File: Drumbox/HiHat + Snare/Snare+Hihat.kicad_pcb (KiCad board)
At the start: 2 copper layers, 127.5 x 133 mm, 81 parts, among them J1 Snare IN, J2 Power Input, J3 HiHat IN, J4 Snare OUT, J5 Conn_01x08_Male, J6 Conn_01x08_Female, J7 Conn_01x08_Male, J8 Conn_01x08_Female, J9 HiHat OUT, Q1 BC546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

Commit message: lots
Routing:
- net GND: vias 10 -> 9

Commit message: finish snare + hihat
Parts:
- added REF**: Doepfer Mounting hole, Synth:Doepfer Mounting hole, F.Cu at (148.5, 22.5)
- added REF**: Doepfer Mounting hole, Synth:Doepfer Mounting hole, F.Cu at (127.0, 22.5)
- added REF**: Doepfer Mounting hole, Synth:Doepfer Mounting hole, F.Cu at (126.5, 149.5)
- added REF**: Doepfer Mounting hole, Synth:Doepfer Mounting hole, F.Cu at (148.5, 149.5)
- moved C13 0.50 mm to (83.0, 80.5)
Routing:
- net /DeH: track 56.8 -> 69.5 mm
- net /HiO: track 92.2 -> 94.1 mm
- net /SnO: track 80.5 -> 81.5 mm
- net /HiH: track 103.0 -> 103.9 mm
- net Net-(J9-PadT): track 72.7 -> 73.4 mm
- net GND: vias 9 -> 2
- net (no net): vias 7 -> 12
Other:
- outline, holes or cut-outs redrawn
- board text added: "JLCJLCJLCJLC"

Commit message: fix gerber files on ms20 filter + gerber on hihat+snare
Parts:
- moved C10 0.32 mm to (38.4, 66.3)
- moved R7 0.21 mm to (43.6, 63.2)
- moved C19 0.20 mm to (56.7, 69.0)
- moved C21 0.20 mm to (56.7, 66.0)
- moved R8 0.12 mm to (43.6, 60.1)
- moved R10 0.06 mm to (33.4, 57.0)
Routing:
- net /HiO: track 94.1 -> 94.9 mm
- net Net-(C12-Pad1): track 23.6 -> 24.3 mm
- net /HiH: track 103.9 -> 104.5 mm

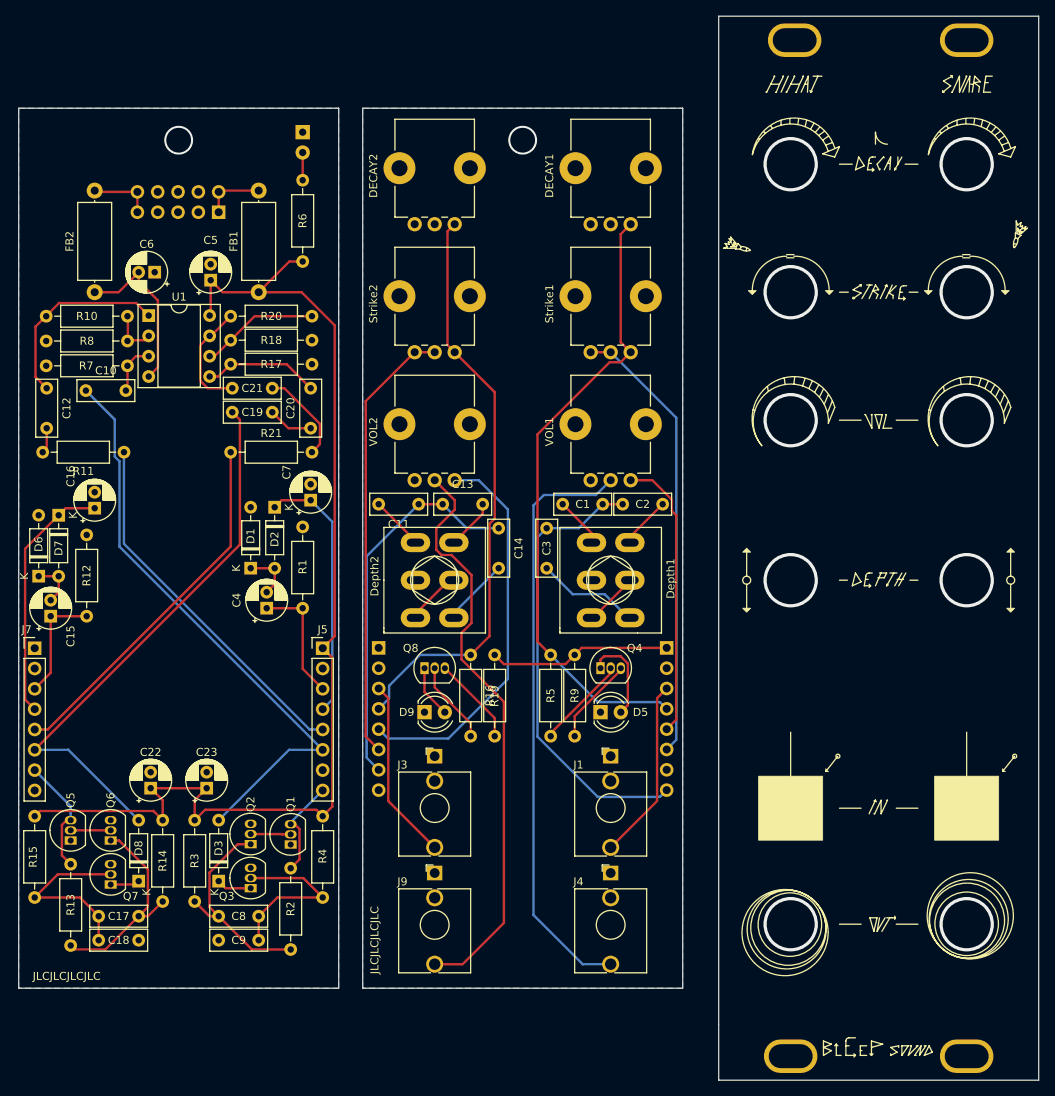
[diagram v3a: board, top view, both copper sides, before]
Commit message: update snare + hihat
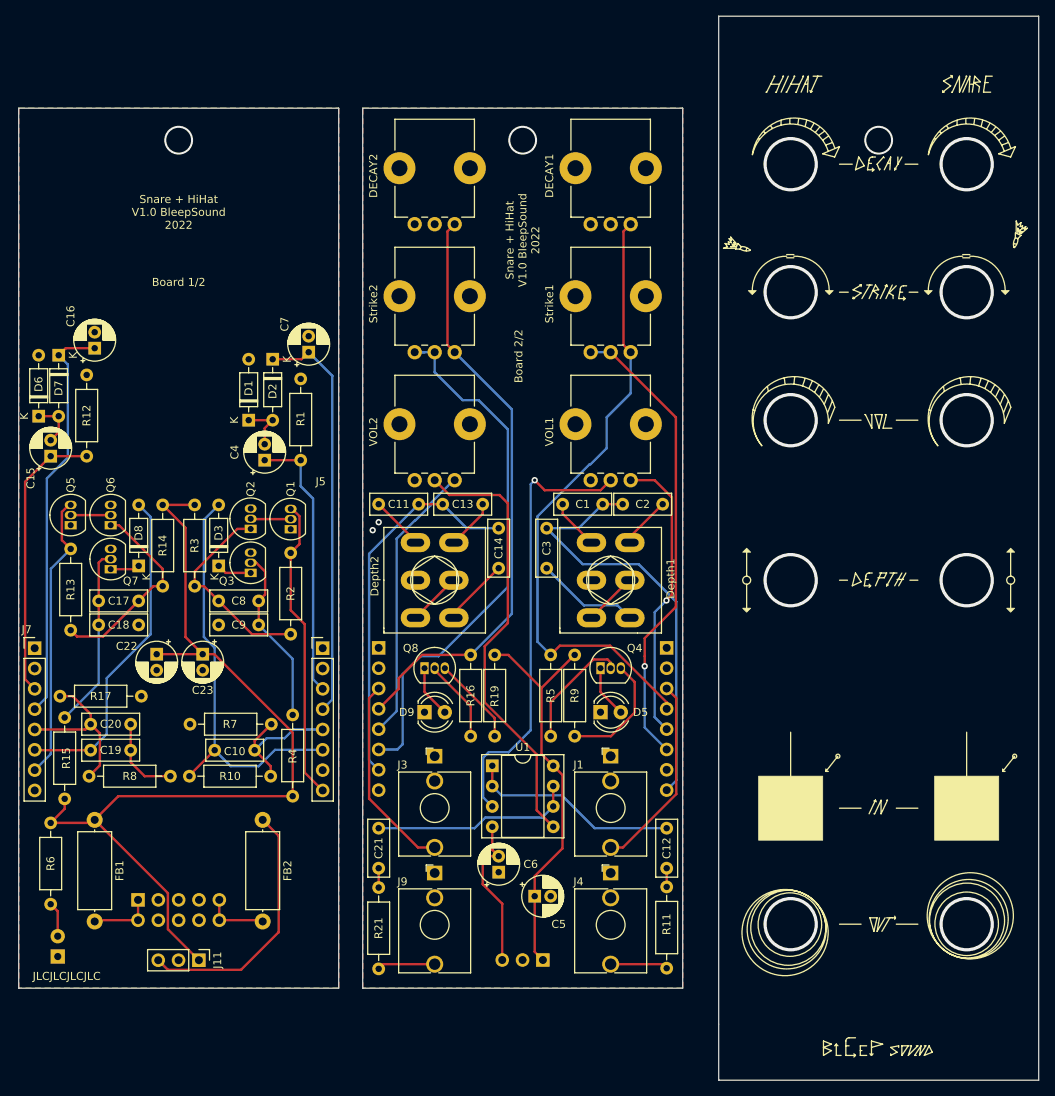
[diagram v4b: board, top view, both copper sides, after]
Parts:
- removed R18: 6.8k, Resistor_THT:R_Axial_DIN0207_L6.3mm_D2.5mm_P10.16mm_Horizontal
- removed R20: 100k, Resistor_THT:R_Axial_DIN0207_L6.3mm_D2.5mm_P10.16mm_Horizontal
- removed REF** (x4): Doepfer Mounting hole, Synth:Doepfer Mounting hole
- added J10: Conn_01x03_Female, Connector_PinSocket_2.54mm:PinSocket_1x03_P2.54mm_Vertical, B.Cu at (95.5, 137.5)
- added J11: Conn_01x03_Male, Connector_PinHeader_2.54mm:PinHeader_1x03_P2.54mm_Vertical, F.Cu at (52.5, 137.5)
- R10: value 100k -> 0R
- R11, R21: value 1M -> 1k
- R8: value 6.8k -> 0R
- moved D4 107.5 mm to (34.9, 137.0), turned to 90 degrees
- moved C12 95.0 mm to (111.0, 121.0)
- moved R11 93.6 mm to (111.0, 138.5), turned to 90 degrees
- moved C5 87.0 mm to (94.5, 129.5), turned to 0 degrees
- moved J2 86.5 mm to (44.9, 130.0), turned to -90 degrees
- moved C6 86.5 mm to (90.0, 126.5), turned to 90 degrees
- moved R6 76.9 mm to (34.0, 120.3), turned to -90 degrees
- moved U1 70.8 mm to (89.2, 113.2)
- moved FB2 69.2 mm to (60.5, 120.0), turned to -90 degrees
- moved FB1 69.1 mm to (39.5, 120.0), turned to -90 degrees
- moved R21 67.2 mm to (75.0, 138.6), turned to 90 degrees
- moved R10 64.0 mm to (61.5, 114.5), turned to 180 degrees
- moved C21 58.0 mm to (75.0, 121.0), turned to -90 degrees
- moved R8 54.6 mm to (38.8, 114.5), turned to 0 degrees
- moved R7 48.3 mm to (61.6, 108.0)
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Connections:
- C10 pad 2: Net-(C10-Pad2) -> /SnO
- C12 pad 1: Net-(C12-Pad1) -> Net-(U1-Pad2)
- C20 pad 2: Net-(C20-Pad2) -> /HiO
- J1 pad TN: Net-(J1-PadTN) -> unconnected-(J1-PadTN)
- J3 pad TN: Net-(J3-PadTN) -> unconnected-(J3-PadTN)
- J4 pad T: Net-(J4-PadT) -> Net-(R11-Pad1)
- J4 pad TN: Net-(J4-PadTN) -> unconnected-(J4-PadTN)
- J5 pad 1: +12V -> GND
- J6 pad 1: +12V -> GND
- J9 pad T: Net-(J9-PadT) -> Net-(R21-Pad1)
- J9 pad TN: Net-(J9-PadTN) -> unconnected-(J9-PadTN)
- Q1 pad 1: Net-(Q1-Pad1) -> unconnected-(Q1-Pad1)
- Q5 pad 1: Net-(Q5-Pad1) -> unconnected-(Q5-Pad1)
- R10 pad 1: Net-(C12-Pad1) -> /SnO
- R10 pad 2: Net-(R10-Pad2) -> /So
- R11 pad 1: /SnO -> Net-(R11-Pad1)
- R17 pad 1: Net-(C20-Pad2) -> /HiO
- R21 pad 1: /HiO -> Net-(R21-Pad1)
- R7 pad 1: Net-(C10-Pad2) -> /SnO
- R8 pad 1: Net-(R10-Pad2) -> /HiO
- R8 pad 2: GND -> Net-(C19-Pad2)
- U1 pad 1: Net-(C12-Pad1) -> Net-(U1-Pad2)
- U1 pad 2: Net-(R10-Pad2) -> Net-(U1-Pad2)
- U1 pad 3: Net-(C10-Pad2) -> Net-(VOL1-Pad2)
- U1 pad 5: Net-(C20-Pad2) -> Net-(VOL2-Pad2)
- U1 pad 6: Net-(R18-Pad1) -> Net-(C21-Pad1)
- VOL1 pad 2: Net-(J4-PadT) -> Net-(VOL1-Pad2)
- VOL2 pad 2: Net-(J9-PadT) -> Net-(VOL2-Pad2)
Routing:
- net Net-(J4-PadT): track 74.4 -> 0.00 mm
- net Net-(J9-PadT): track 73.4 -> 0.00 mm
- net Net-(VOL1-Pad2): track 0.00 -> 55.9 mm, vias 0 -> 1
- net Net-(VOL2-Pad2): track 0.00 -> 55.5 mm
- net /HiO: track 94.9 -> 56.0 mm
- net -12V: track 21.0 -> 51.9 mm
- net /SnO: track 81.5 -> 54.3 mm, vias 0 -> 1
- net Net-(U1-Pad2): track 0.00 -> 26.5 mm
- net Net-(C12-Pad1): track 24.3 -> 0.00 mm
- net /HiI: track 37.2 -> 60.4 mm
- net /DeH: track 69.5 -> 92.7 mm
- net /HiH: track 104.5 -> 126.0 mm
- net /HiDH: track 62.1 -> 83.6 mm
- net /SnI: track 38.4 -> 58.9 mm
- net /So: track 129.9 -> 110.0 mm, vias 0 -> 1
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- added copper zone on F.Cu, net GND
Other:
- net class Default removed
- net class Power removed
- board text added: "Board 1/2"
- board text added: "Board 2/2"
- board text added: "Snare + HiHat V1.0 BleepSound 2022"

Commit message: gerber files for snare + hihat
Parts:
- added REF**: Doepfer Mounting hole, Synth:Doepfer Mounting hole, F.Cu at (150.0, 149.5)
- added REF**: Doepfer Mounting hole, Synth:Doepfer Mounting hole, F.Cu at (124.5, 22.5)
- added REF**: Doepfer Mounting hole, Synth:Doepfer Mounting hole, F.Cu at (150.0, 22.5)
- added REF**: Doepfer Mounting hole, Synth:Doepfer Mounting hole, F.Cu at (125.0, 149.5)
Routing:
- net /Ho: track 109.2 -> 107.9 mm
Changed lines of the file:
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@@
       (effects (font (size 1 1) (thickness 0.15)))
     )
-    (fp_text user "K" (at 0 -1.8 90) (layer "F.SilkS")
+    (fp_text user "K" (at 0.62 -1.8 90) (layer "F.SilkS")
       (effects (font (size 1 1) (thickness 0.15)))
     )
@@
     (fp_line (start -1.45 2.75) (end 4 2.75) (layer "F.CrtYd") (width 0.05))
     (fp_line (start -0.73 -1.32665) (end -0.73 1.32665) (layer "F.Fab") (width 0.1))
-    (fp_arc (start -0.73 -1.32665) (mid 3.67 0.000306) (end -0.730339 1.32614) (layer "F.Fab") (width 0.1))
+    (fp_arc (start -0.73 -1.32665) (mid 3.670001 0.000308) (end -0.730339 1.32614) (layer "F.Fab") (width 0.1))
     (fp_circle (center 1.27 0) (end 3.27 0) (layer "F.Fab") (width 0.1) (fill none))
     (pad "1" thru_hole rect locked (at 0 0) (size 1.8 1.8) (drill 0.9) (layers *.Cu *.Mask)
@@
       (effects (font (size 1 1) (thickness 0.15)))
     )
-    (fp_text user "K" (at 0 -1.8 90) (layer "F.SilkS")
+    (fp_text user "K" (at 1.12 -1.8 90) (layer "F.SilkS")
       (effects (font (size 1 1) (thickness 0.15)))
     )
@@
     (fp_line (start 4 2.75) (end 4 -2.75) (layer "F.CrtYd") (width 0.05))
     (fp_line (start -0.73 -1.32665) (end -0.73 1.32665) (layer "F.Fab") (width 0.1))
-    (fp_arc (start -0.73 -1.32665) (mid 3.67 0.000306) (end -0.730339 1.32614) (layer "F.Fab") (width 0.1))
+    (fp_arc (start -0.73 -1.32665) (mid 3.670001 0.000308) (end -0.730339 1.32614) (layer "F.Fab") (width 0.1))
     (fp_circle (center 1.27 0) (end 3.27 0) (layer "F.Fab") (width 0.1) (fill none))
     (pad "1" thru_hole rect locked (at 0 0) (size 1.8 1.8) (drill 0.9) (layers *.Cu *.Mask)
@@
     (property "Sheetname" "")
     (attr through_hole)
-    (fp_text reference "DECAY1" (at 6.05 -10.15 90) (layer "F.SilkS")
+    (fp_text reference "DECAY1" (at 1.5 -9.5 90) (layer "F.SilkS")
       (effects (font (size 1 1) (thickness 0.15)))
     )
@@
     )
   )
+  (footprint "Synth:Doepfer Mounting hole" (layer "F.Cu")
+    (at 150 149.5)
+    (attr through_hole)
+    (fp_text reference "REF**" (at 0 3) (layer "F.SilkS") hide
+      (effects (font (size 1 1) (thickness 0.15)))
+    )
+    (fp_text value "Doepfer Mounting hole" (at 0 -3) (layer "F.Fab")
+      (effects (font (size 1 1) (thickness 0.15)))
+    )
+    (pad "1" thru_hole oval locked (at 0 0) (size 6.7 4.2) (drill oval 5.5 3) (layers *.Cu *.Mask))
+  )
+  (footprint "Synth:Doepfer Mounting hole" (layer "F.Cu")
+    (at 124.5 22.5)
+    (attr through_hole)
+    (fp_text reference "REF**" (at 0 3) (layer "F.SilkS") hide
+      (effects (font (size 1 1) (thickness 0.15)))
+    )
+    (fp_text value "Doepfer Mounting hole" (at 0 -3) (layer "F.Fab")
+      (effects (font (size 1 1) (thickness 0.15)))
+    )
+    (pad "1" thru_hole oval locked (at 0 0) (size 6.7 4.2) (drill oval 5.5 3) (layers *.Cu *.Mask))
+  )
   (footprint "Resistor_THT:R_Axial_DIN0207_L6.3mm_D2.5mm_P10.16mm_Horizontal" (layer "F.Cu")
     (at 61.5 114.5 180)
@@
     )
   )
+  (footprint "Synth:Doepfer Mounting hole" (layer "F.Cu")
+    (at 150 22.5)
+    (attr through_hole)
+    (fp_text reference "REF**" (at 0 3) (layer "F.SilkS") hide
+      (effects (font (size 1 1) (thickness 0.15)))
+    )
+    (fp_text value "Doepfer Mounting hole" (at 0 -3) (layer "F.Fab")
+      (effects (font (size 1 1) (thickness 0.15)))
+    )
+    (pad "1" thru_hole oval locked (at 0 0) (size 6.7 4.2) (drill oval 5.5 3) (layers *.Cu *.Mask))
+  )
+  (footprint "Synth:Doepfer Mounting hole" (layer "F.Cu")
+    (at 125 149.5)
+    (attr through_hole)
+    (fp_text reference "REF**" (at 0 3) (layer "F.SilkS") hide
+      (effects (font (size 1 1) (thickness 0.15)))
+    )
+    (fp_text value "Doepfer Mounting hole" (at 0 -3) (layer "F.Fab")
+      (effects (font (size 1 1) (thickness 0.15)))
+    )
+    (pad "1" thru_hole oval locked (at 0 0) (size 6.7 4.2) (drill oval 5.5 3) (layers *.Cu *.Mask))
+  )
   (footprint "LED_THT:LED_D4.0mm" (layer "B.Cu")
     (at 34.88 137.04 90)
@@
     (fp_line (start 4 -2.75) (end 4 2.75) (layer "B.CrtYd") (width 0.05))
     (fp_line (start -0.73 1.32665) (end -0.73 -1.32665) (layer "B.Fab") (width 0.1))
-    (fp_arc (start -0.730339 -1.32614) (mid 3.670001 -0.000306) (end -0.73 1.32665) (layer "B.Fab") (width 0.1))
+    (fp_arc (start -0.730339 -1.32614) (mid 3.67 -0.000308) (end -0.73 1.32665) (layer "B.Fab") (width 0.1))
     (fp_circle (center 1.27 0) (end 3.27 0) (layer "B.Fab") (width 0.1) (fill none))
     (pad "1" thru_hole rect locked (at 0 0 90) (size 1.8 1.8) (drill 0.9) (layers *.Cu *.Mask)
@@
     (effects (font (size 1 1) (thickness 0.15)))
   )
-  (gr_text "Snare + HiHat\nV1.0 BleepSound\n2022" (at 50 44) (layer "F.SilkS")
+  (gr_text "Snare + HiHat\nV1.0 BleepSound\n2022" (at 50 40) (layer "F.SilkS")
     (effects (font (size 1 1) (thickness 0.15)))
   )
-  (gr_text "Snare + HiHat\nV1.0 BleepSound\n2022" (at 93 47.5 90) (layer "F.SilkS")
+  (gr_text "Snare + HiHat\nV1.0 BleepSound\n2022" (at 93 38 90) (layer "F.SilkS")
     (effects (font (size 1 1) (thickness 0.15)))
   )
@@
   (via (at 148.5 38) (size 6.8) (drill 6) (layers "F.Cu" "B.Cu") (net 0))
   (via (at 126.5 70) (size 6.8) (drill 6) (layers "F.Cu" "B.Cu") (net 0))
-  (via (at 137.5 35) (size 3.6) (drill 3.1) (layers "F.Cu" "B.Cu") (free) (net 0))
+  (via (at 137.5 47) (size 3.6) (drill 3.1) (layers "F.Cu" "B.Cu") (free) (net 0))
   (via (at 126.5 90) (size 6.8) (drill 6) (layers "F.Cu" "B.Cu") (net 0))
   (via (at 126.5 54) (size 6.8) (drill 6) (layers "F.Cu" "B.Cu") (net 0))
-  (via (at 50 35) (size 3.6) (drill 3.1) (layers "F.Cu" "B.Cu") (net 1))
-  (via (at 93 35) (size 3.6) (drill 3.1) (layers "F.Cu" "B.Cu") (net 1))
+  (via (at 50 47) (size 3.6) (drill 3.1) (layers "F.Cu" "B.Cu") (net 1))
+  (via (at 93 47) (size 3.6) (drill 3.1) (layers "F.Cu" "B.Cu") (net 1))
   (via (at 75 82.75) (size 0.8) (drill 0.4) (layers "F.Cu" "B.Cu") (free) (net 1))
   (via (at 74.25 83.75) (size 0.8) (drill 0.4) (layers "F.Cu" "B.Cu") (free) (net 1))
@@
   (segment (start 39 111.25) (end 32.05 111.25) (width 0.3) (layer "F.Cu") (net 30))
   (segment (start 32.05 111.25) (end 32 111.2) (width 0.3) (layer "F.Cu") (net 30))
-  (segment (start 79.5 61.5) (end 80.772792 61.5) (width 0.3) (layer "B.Cu") (net 30))
   (segment (start 82.5 99.5) (end 91.149511 90.850489) (width 0.3) (layer "B.Cu") (net 30))
   (segment (start 87.5 67.5) (end 85.5 67.5) (width 0.3) (layer "B.Cu") (net 30))
   (segment (start 78 101.755978) (end 78.127989 101.627989) (width 0.3) (layer "B.Cu") (net 30))
   (segment (start 75 111.16) (end 77.34 111.16) (width 0.3) (layer "B.Cu") (net 30))
-  (segment (start 79.5 61.5) (end 82 61.5) (width 0.3) (layer "B.Cu") (net 30))
   (segment (start 45 80.59) (end 46.5 82.09) (width 0.3) (layer "B.Cu") (net 30))
+  (segment (start 82 61.5) (end 79.5 61.5) (width 0.3) (layer "B.Cu") (net 30))
   (segment (start 80.255978 99.5) (end 82.5 99.5) (width 0.3) (layer "B.Cu") (net 30))
   (segment (start 41 102.25) (end 41 109.25) (width 0.3) (layer "B.Cu") (net 30))
